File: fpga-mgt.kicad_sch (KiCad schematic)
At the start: 50 parts, among them U34 XCAU25P-2FFVB676I, U39 SI5319C-C-GM-ND, Y4 Resonator_114.285MHZ_ABM8

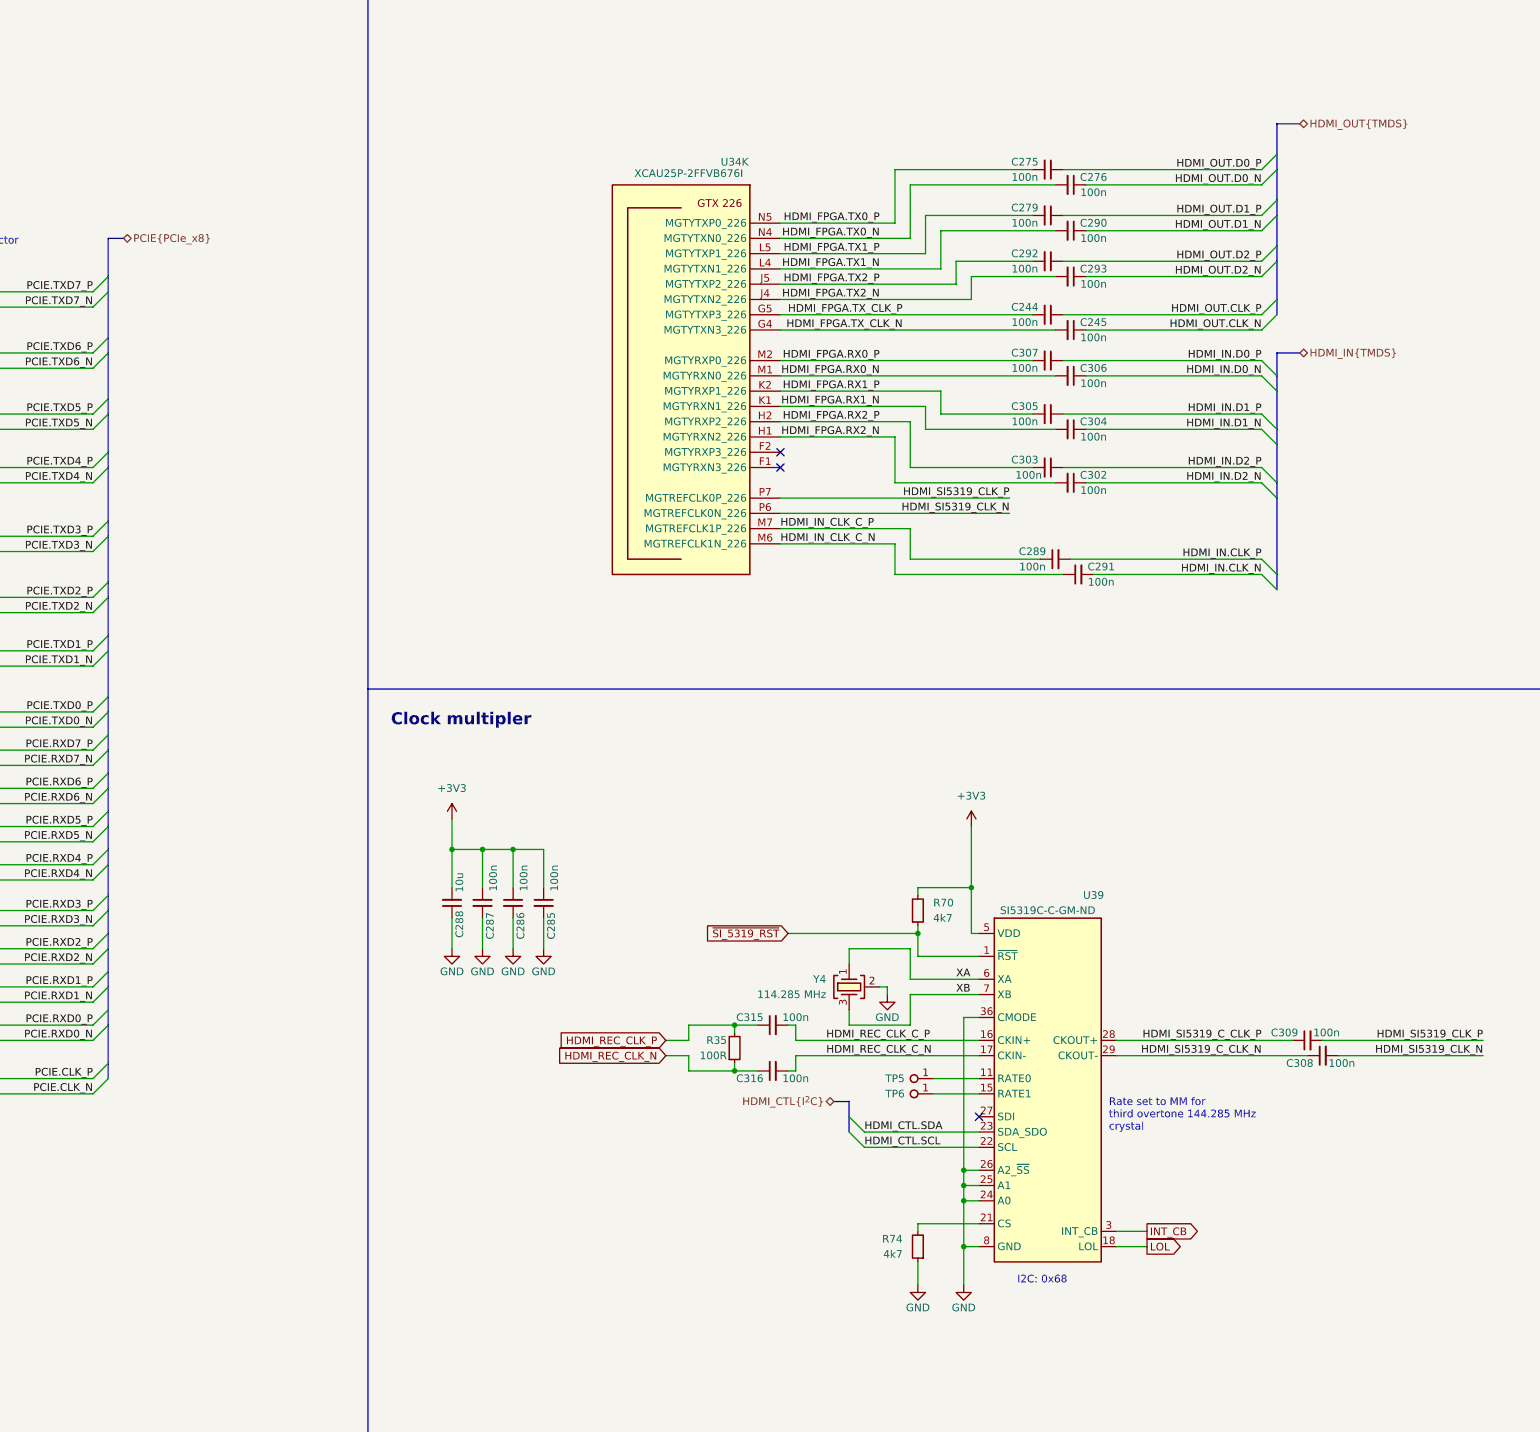
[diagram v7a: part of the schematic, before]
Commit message: [#68016] Improve bus entry marking
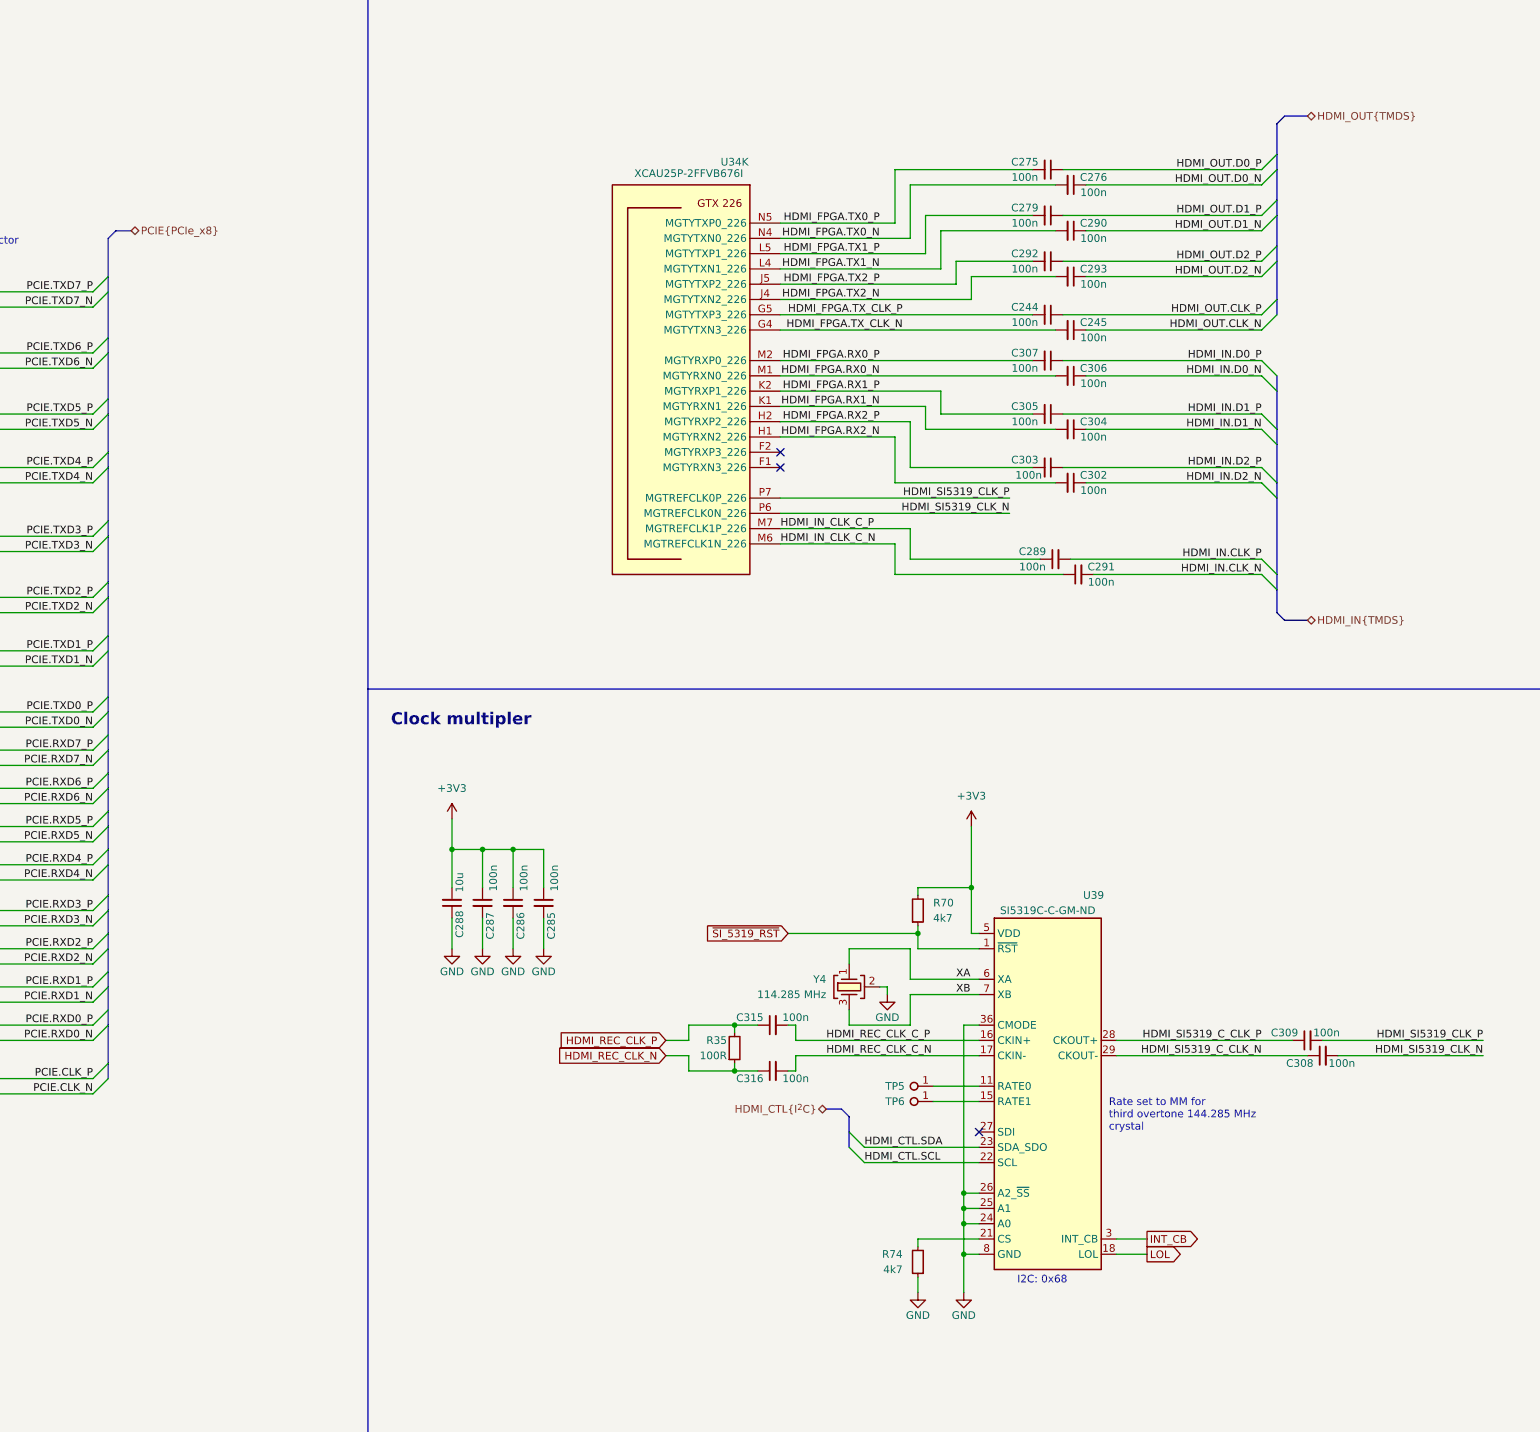
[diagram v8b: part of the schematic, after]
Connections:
- net GND: now also U39.37 (GND)
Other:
- moved on the sheet: R74, TP5, TP6, U39
